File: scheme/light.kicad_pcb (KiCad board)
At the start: 2 copper layers, 25 parts, among them J1 Screw_Terminal_01x04 (buttons), J2 Conn_01x06_Male (programmer), J3 Screw_Terminal_01x06 (output), J4 Conn_01x02_Male (i2c), J5 Conn_01x02_Male (Jumper), J6 Conn_01x03_Male (Indicators), J7 Screw_Terminal_01x02 (power), Q1 IRF8308M, Q2 IRF8308M, Q3 IRF8308M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

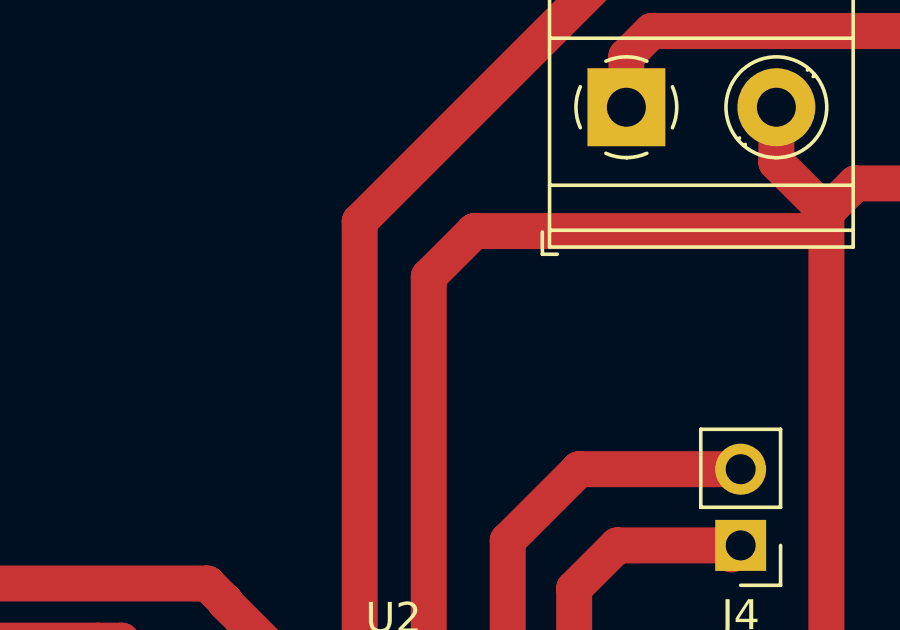
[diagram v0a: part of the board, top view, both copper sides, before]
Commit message: cheme: add marks layer
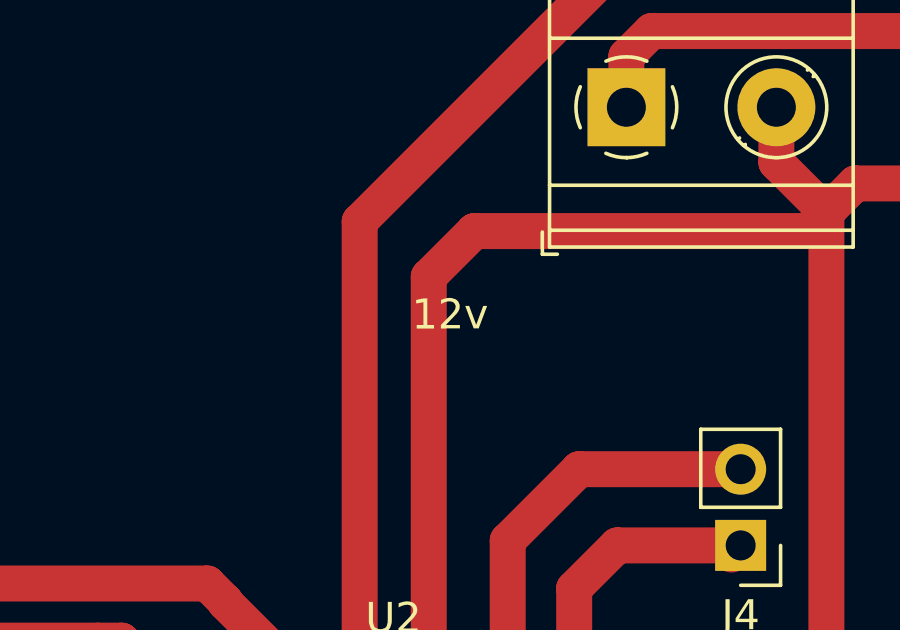
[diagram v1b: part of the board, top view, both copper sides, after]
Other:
- board text added: "+"
- board text added: "-"
- board text added: "1"
- board text added: "100Ohm"
- board text added: "10kOhm"
- board text added: "12v"
- board text added: "2"
- board text added: "220Ohm"
- board text added: "3"
- board text added: "5v +"
- board text added: "Buttons"
- board text added: "GND"
- board text added: "Info OUT"
- board text added: "Jumper"
- board text added: "MISO"
- board text added: "MOSI"
- board text added: "Max 40v, Max 30 A"
- board text added: "Normally: ON Programmer: OFF"
- board text added: "Pwr OUT"
- board text added: "Reset"
- board text added: "SCK"
- board text added: "SCL"
- board text added: "SDA"
- board text added: "TWP"
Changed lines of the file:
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@@
   (general
     (thickness 1.6)
-    (drawings 8)
+    (drawings 58)
     (tracks 220)
     (zones 0)
@@
   (page A4)
   (layers
-    (0 F.Cu signal)
-    (31 B.Cu signal)
+    (0 F.Cu signal hide)
+    (31 B.Cu signal hide)
     (32 B.Adhes user hide)
     (33 F.Adhes user hide)
@@
     (35 F.Paste user hide)
     (36 B.SilkS user)
-    (37 F.SilkS user)
+    (37 F.SilkS user hide)
     (38 B.Mask user hide)
     (39 F.Mask user hide)
@@
     (45 Margin user hide)
     (46 B.CrtYd user hide)
-    (47 F.CrtYd user hide)
+    (47 F.CrtYd user)
     (48 B.Fab user hide)
     (49 F.Fab user hide)
   )
   (setup
-    (last_trace_width 1.2)
+    (last_trace_width 0.4)
     (user_trace_width 0.6)
     (user_trace_width 0.8)
@@
     )
   )
+  (gr_text 220Ohm (at 183.228 90.772 90) (layer F.CrtYd)
+    (effects (font (size 1 1) (thickness 0.15)))
+  )
+  (gr_text 220Ohm (at 176.878 90.772 90) (layer F.CrtYd)
+    (effects (font (size 1 1) (thickness 0.15)))
+  )
+  (gr_text 220Ohm (at 171.036 91.026 90) (layer F.CrtYd)
+    (effects (font (size 1 1) (thickness 0.15)))
+  )
+  (gr_text 10kOhm (at 163.924 120.998) (layer F.CrtYd)
+    (effects (font (size 1 1) (thickness 0.15)))
+  )
+  (gr_text 100Ohm (at 133.698 130.65) (layer F.CrtYd)
+    (effects (font (size 1 1) (thickness 0.15)))
+  )
+  (gr_text 100Ohm (at 143.858 106.52) (layer F.CrtYd)
+    (effects (font (size 1 1) (thickness 0.15)))
+  )
+  (gr_text 100Ohm (at 144.112 95.09) (layer F.CrtYd)
+    (effects (font (size 1 1) (thickness 0.15)))
+  )
+  (gr_text 10kOhm (at 124.046 121.506 90) (layer F.CrtYd)
+    (effects (font (size 1 1) (thickness 0.15)))
+  )
+  (gr_text 10kOhm (at 124.046 107.282 90) (layer F.CrtYd)
+    (effects (font (size 1 1) (thickness 0.15)))
+  )
+  (gr_text 10kOhm (at 124.046 93.312 90) (layer F.CrtYd)
+    (effects (font (size 1 1) (thickness 0.15)))
+  )
+  (gr_text Reset (at 143.35 112.616) (layer F.CrtYd)
+    (effects (font (size 1 1) (thickness 0.15)))
+  )
+  (gr_text SCK (at 165.448 134.968 90) (layer F.CrtYd)
+    (effects (font (size 1 1) (thickness 0.15)))
+  )
+  (gr_text MISO (at 162.908 134.968 90) (layer F.CrtYd)
+    (effects (font (size 1 1) (thickness 0.15)))
+  )
+  (gr_text MOSI (at 160.368 134.968 90) (layer F.CrtYd)
+    (effects (font (size 1 1) (thickness 0.15)))
+  )
+  (gr_text Reset (at 157.828 134.968 90) (layer F.CrtYd)
+    (effects (font (size 1 1) (thickness 0.15)))
+  )
+  (gr_text GND (at 155.034 134.968 90) (layer F.CrtYd)
+    (effects (font (size 1 1) (thickness 0.15)))
+  )
+  (gr_text "5v +" (at 152.494 134.968 90) (layer F.CrtYd)
+    (effects (font (size 1 1) (thickness 0.15)))
+  )
+  (gr_text "Normally: ON\nProgrammer: OFF" (at 134.46 139.286) (layer F.CrtYd)
+    (effects (font (size 1 1) (thickness 0.15)))
+  )
+  (gr_text Jumper (at 144.874 135.73) (layer F.CrtYd)
+    (effects (font (size 1 1) (thickness 0.15)))
+  )
+  (gr_text GND (at 106.266 91.026) (layer F.CrtYd)
+    (effects (font (size 1 1) (thickness 0.15)))
+  )
+  (gr_text "Max 40v, Max 30 A" (at 107.536 88.994) (layer F.CrtYd)
+    (effects (font (size 1 1) (thickness 0.15)))
+  )
+  (gr_text "Pwr OUT" (at 106.266 86.2) (layer F.CrtYd)
+    (effects (font (size 1 1) (thickness 0.15)))
+  )
+  (gr_text 3 (at 112.616 118.966) (layer F.CrtYd)
+    (effects (font (size 1 1) (thickness 0.15)))
+  )
+  (gr_text 2 (at 112.616 108.044) (layer F.CrtYd)
+    (effects (font (size 1 1) (thickness 0.15)))
+  )
+  (gr_line (start 114.14 113.632) (end 114.14 113.378) (layer F.CrtYd) (width 0.05))
+  (gr_line (start 100.17 113.632) (end 114.14 113.632) (layer F.CrtYd) (width 0.05))
+  (gr_line (start 114.14 124.3) (end 100.085 124.24) (layer F.CrtYd) (width 0.05))
+  (gr_line (start 114.14 103.218) (end 114.14 124.3) (layer F.CrtYd) (width 0.05))
+  (gr_text 1 (at 112.616 98.392) (layer F.CrtYd)
+    (effects (font (size 1 1) (thickness 0.15)))
+  )
+  (gr_text "5v +" (at 141.064 78.58) (layer F.CrtYd)
+    (effects (font (size 1 1) (thickness 0.15)))
+  )
+  (gr_line (start 114.14 103.218) (end 100.17 103.218) (layer F.CrtYd) (width 0.05))
+  (gr_line (start 114.14 92.76) (end 114.14 103.218) (layer F.CrtYd) (width 0.05))
+  (gr_line (start 100.085 92.76) (end 114.14 92.76) (layer F.CrtYd) (width 0.05))
+  (gr_text 3 (at 137.254 86.962) (layer F.CrtYd)
+    (effects (font (size 1 1) (thickness 0.15)))
+  )
+  (gr_text 2 (at 137.254 84.422) (layer F.CrtYd)
+    (effects (font (size 1 1) (thickness 0.15)))
+  )
+  (gr_text 1 (at 137.254 81.628) (layer F.CrtYd)
+    (effects (font (size 1 1) (thickness 0.15)))
+  )
+  (gr_text "Info OUT" (at 141.318 76.04) (layer F.CrtYd)
+    (effects (font (size 1 1) (thickness 0.15)))
+  )
+  (gr_text SCL (at 172.56 78.58) (layer F.CrtYd)
+    (effects (font (size 1 1) (thickness 0.15)))
+  )
+  (gr_text SDA (at 172.56 76.04) (layer F.CrtYd)
+    (effects (font (size 1 1) (thickness 0.15)))
+  )
+  (gr_text "TWP\n" (at 162.654 77.31) (layer F.CrtYd)
+    (effects (font (size 1 1) (thickness 0.15)))
+  )
+  (gr_text Buttons (at 194.404 81.628) (layer F.CrtYd)
+    (effects (font (size 1 1) (thickness 0.15)))
+  )
+  (gr_text 3 (at 187.8 102.202) (layer F.CrtYd)
+    (effects (font (size 1 1) (thickness 0.15)))
+  )
+  (gr_text 2 (at 187.8 97.122) (layer F.CrtYd)
+    (effects (font (size 1 1) (thickness 0.15)))
+  )
+  (gr_text 1 (at 187.8 91.534) (layer F.CrtYd)
+    (effects (font (size 1 1) (thickness 0.15)))
+  )
+  (gr_text + (at 187.8 86.454) (layer F.CrtYd)
+    (effects (font (size 1 1) (thickness 0.15)))
+  )
+  (gr_text 12v (at 157.828 64.356) (layer F.CrtYd)
+    (effects (font (size 1 1) (thickness 0.15)))
+  )
+  (gr_text 12v (at 158.336 70.96) (layer F.SilkS)
+    (effects (font (size 1 1) (thickness 0.15)))
+  )
+  (gr_text - (at 169.766 70.452) (layer F.CrtYd)
+    (effects (font (size 1 1) (thickness 0.15)))
+  )
+  (gr_text + (at 163.924 70.452) (layer F.CrtYd)
+    (effects (font (size 1 1) (thickness 0.15)))
+  )
+  (gr_text + (at 163.67 71.468) (layer F.Paste)
+    (effects (font (size 1 1) (thickness 0.15)))
+  )
   (gr_circle (center 193 143) (end 196.2 143) (layer F.Cu) (width 2))
